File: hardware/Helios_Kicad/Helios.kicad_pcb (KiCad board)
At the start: 2 copper layers, 75 x 61 mm, 95 parts, among them P1 USB_B, P2 CONN_01X25-SHIELD, P3 CONN_01X03, U1 IP4220CZ6, U2 AP2114, U3 AN431B, U4 ISA_DC-DC_converter, U5 DAC084S085C, U6 TL084_v, U7 LM358, U8 TL084_v, U9 ATSAM4S, Y1 16MHz 18pF

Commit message: driver finished but untested
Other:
- board text added: "EMIT"
- board text removed: "LASER"
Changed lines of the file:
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@@
-(kicad_pcb (version 4) (host pcbnew 4.0.2-stable)
+(kicad_pcb (version 4) (host pcbnew 4.0.1-stable)
   (general
     (links 218)
@@
   )
   (setup
-    (last_trace_width 0.5)
+    (last_trace_width 0.35)
     (user_trace_width 0.25)
     (user_trace_width 0.35)
@@
       (solder_mask_margin 0.77) (clearance 0.77))
   )
-  (gr_line (start 101.1 117.5) (end 100.9 117.5) (angle 90) (layer F.SilkS) (width 0.2))
-  (gr_line (start 108.5 117.5) (end 101.1 117.5) (angle 90) (layer F.SilkS) (width 0.2))
-  (gr_line (start 108.5 123.3) (end 108.5 117.5) (angle 90) (layer F.SilkS) (width 0.2))
+  (gr_line (start 107 117.6) (end 107 118.2) (angle 90) (layer F.SilkS) (width 0.2))
+  (gr_line (start 107 117.6) (end 101 117.6) (angle 90) (layer F.SilkS) (width 0.2))
+  (gr_line (start 106.976 123.808) (end 106.976 118.008) (angle 90) (layer F.SilkS) (width 0.2))
   (gr_line (start 106.5 145.5) (end 106.5 139.4) (angle 90) (layer F.SilkS) (width 0.2))
   (gr_line (start 101 145.5) (end 106.5 145.5) (angle 90) (layer F.SilkS) (width 0.2))
-  (gr_text LASER (at 104.4 119.3) (layer F.SilkS)
+  (gr_text EMIT (at 103.6 119.4) (layer F.SilkS)
     (effects (font (size 1.5 1.5) (thickness 0.3)))
   )
@@
   (segment (start 123.6 111.2) (end 127.96 111.2) (width 0.6) (layer F.Cu) (net 4))
   (segment (start 127.96 111.2) (end 128.04 111.28) (width 0.6) (layer F.Cu) (net 4))
-  (segment (start 118.6 112.3) (end 122.3 112.3) (width 0.6) (layer F.Cu) (net 4))
-  (segment (start 122.3 112.3) (end 123.4 111.2) (width 0.6) (layer F.Cu) (net 4))
+  (segment (start 118.6 112.3) (end 122.3 112.3) (width 0.5) (layer F.Cu) (net 4))
+  (segment (start 122.3 112.3) (end 123.4 111.2) (width 0.5) (layer F.Cu) (net 4))
   (segment (start 123.4 111.2) (end 123.6 111.2) (width 0.6) (layer F.Cu) (net 4))
   (segment (start 118.6 111) (end 118.6 112.3) (width 0.6) (layer F.Cu) (net 4))

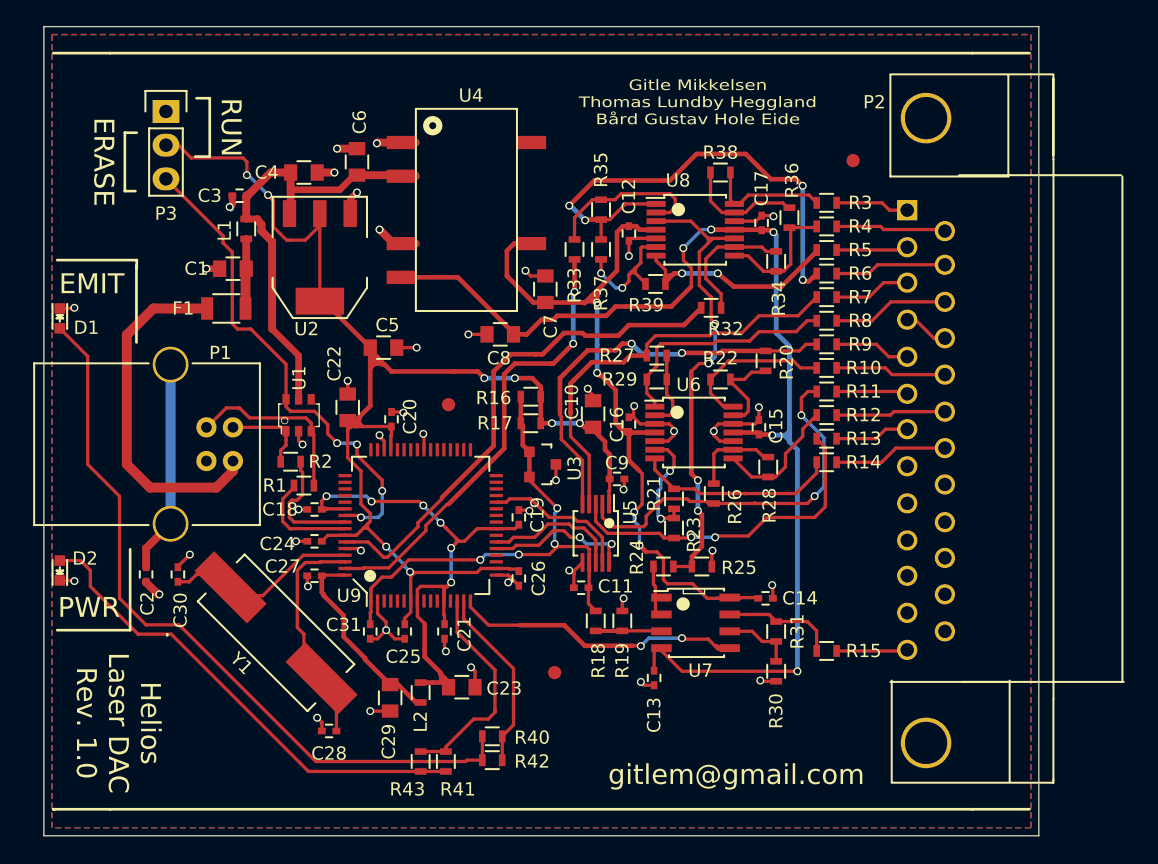
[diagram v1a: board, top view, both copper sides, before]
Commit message: GPIO signal wiring and USB IDs
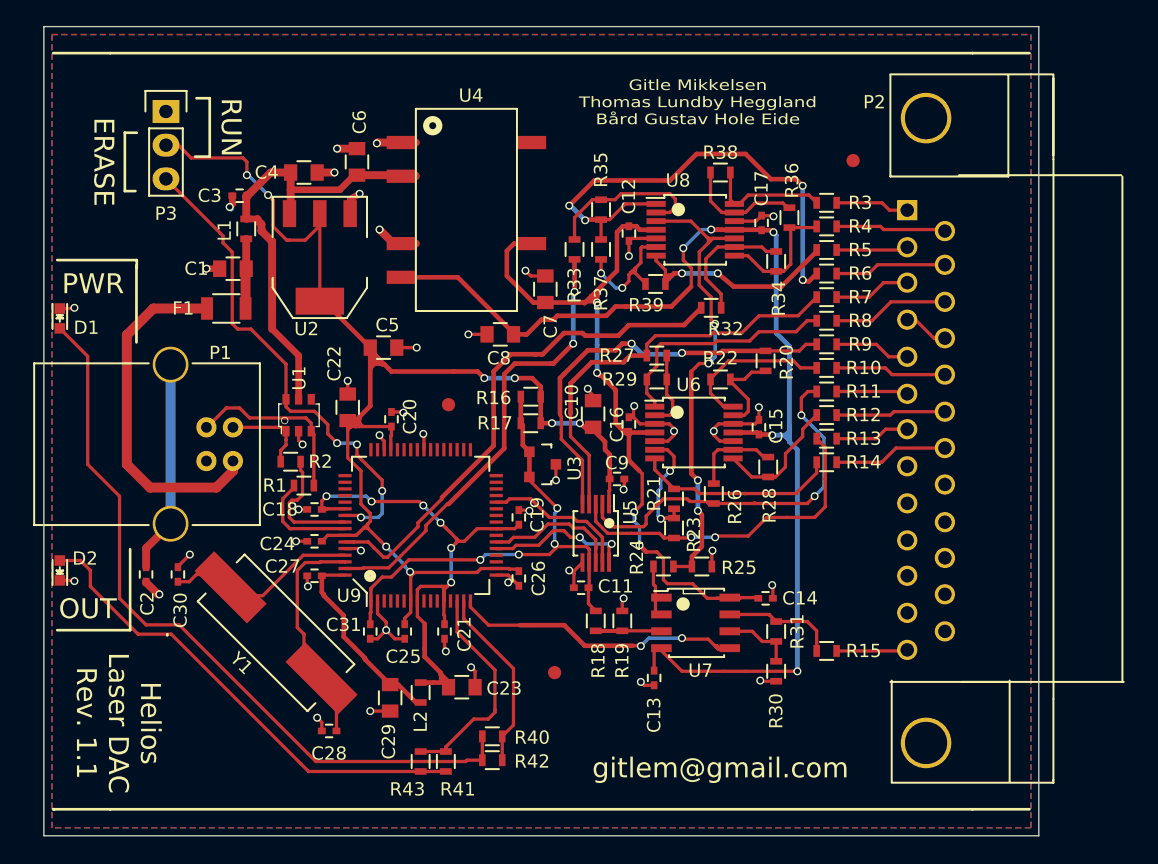
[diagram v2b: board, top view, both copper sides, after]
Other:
- board text added: "Helios Laser DAC Rev. 1.1"
- board text added: "OUT"
- board text removed: "EMIT"
- board text removed: "Helios Laser DAC Rev. 1.0"
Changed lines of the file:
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@@
-(kicad_pcb (version 4) (host pcbnew 4.0.1-stable)
+(kicad_pcb (version 4) (host pcbnew 4.0.2-stable)
   (general
     (links 218)
@@
   )
   (setup
-    (last_trace_width 0.35)
+    (last_trace_width 0.25)
     (user_trace_width 0.25)
     (user_trace_width 0.35)
@@
   (gr_line (start 106.5 145.5) (end 106.5 139.4) (angle 90) (layer F.SilkS) (width 0.2))
   (gr_line (start 101 145.5) (end 106.5 145.5) (angle 90) (layer F.SilkS) (width 0.2))
-  (gr_text EMIT (at 103.6 119.4) (layer F.SilkS)
+  (gr_text OUT (at 103.3 143.9) (layer F.SilkS)
     (effects (font (size 1.5 1.5) (thickness 0.3)))
   )
   (gr_line (start 109.3 145.9) (end 109.3 145.8) (angle 90) (layer F.SilkS) (width 0.2))
-  (gr_text PWR (at 103.4 143.8) (layer F.SilkS)
+  (gr_text PWR (at 103.7 119.4) (layer F.SilkS)
     (effects (font (size 1.5 1.5) (thickness 0.3)))
   )
-  (gr_text gitlem@gmail.com (at 152.2 156.4) (layer F.SilkS)
+  (gr_text gitlem@gmail.com (at 151 155.9) (layer F.SilkS)
     (effects (font (size 1.5 1.5) (thickness 0.3)))
   )
@@
   (gr_line (start 105 159) (end 100.7 159) (angle 90) (layer F.SilkS) (width 0.2))
   (gr_line (start 105 102) (end 100.7 102) (angle 90) (layer F.SilkS) (width 0.2))
-  (gr_text "Helios\nLaser DAC\nRev. 1.0" (at 105.6 152.5 270) (layer F.SilkS)
+  (gr_text "Helios\nLaser DAC\nRev. 1.1" (at 105.6 152.5 270) (layer F.SilkS)
     (effects (font (size 1.5 1.5) (thickness 0.3)))
   )
@@
   (segment (start 115.25 118.25) (end 115.25 116) (width 0.6) (layer F.Cu) (net 1))
   (segment (start 123.086 114.098) (end 123.086 113.014) (width 0.5) (layer F.Cu) (net 2))
-  (via (at 123.6 112.5) (size 0.6) (drill 0.4) (layers F.Cu B.Cu) (net 2))
-  (segment (start 123.086 113.014) (end 123.6 112.5) (width 0.5) (layer F.Cu) (net 2))
+  (via (at 123.8 112.6) (size 0.6) (drill 0.4) (layers F.Cu B.Cu) (net 2))
+  (segment (start 123.086 113.014) (end 123.8 112.6) (width 0.5) (layer F.Cu) (net 2))
   (via (at 112.25 118.25) (size 0.6) (drill 0.4) (layers F.Cu B.Cu) (net 2))
   (segment (start 112.25 118.25) (end 112.3 118.2) (width 0.5) (layer B.Cu) (net 2))

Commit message: redone pcb, driver and firmware working-ish
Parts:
- removed ? (x3): Fiducial_1mm_Dia_2.54mm_Outer_CopperTop, Fiducials:Fiducial_1mm_Dia_2.54mm_Outer_CopperTop
- removed P3: CONN_01X03, Pin_Headers:Pin_Header_Straight_1x03
- added C32: 13pF, Capacitors_SMD:C_0402, F.Cu at (124.8, 145.8)
- added ERASE: CONN_01X02, Connect:PINHEAD1-2, F.Cu at (122.7, 128.2)
- added L3: FILTER, Resistors_SMD:R_0603, F.Cu at (127.0, 149.2)
- added R44: 10k, Resistors_SMD:R_0603, F.Cu at (157.1, 114.9)
- added R45: 1.65k, Resistors_SMD:R_0603, F.Cu at (109.9, 153.6)
- added R46: 1.65k, Resistors_SMD:R_0603, F.Cu at (109.9, 151.7)
- added R47: 1.65k, Resistors_SMD:R_0603, F.Cu at (106.0, 147.3)
- added R48: 1.65k, Resistors_SMD:R_0603, F.Cu at (106.0, 145.5)
- C1, C23, C4, C5, C6, C8: footprint Capacitors_SMD:C_0805 -> Capacitors_SMD:C_0603
- C10, C22, C7: value 4.7uF -> 100nF; footprint Capacitors_SMD:C_0805 -> Capacitors_SMD:C_0402
- C11, C30: value 13pF -> 4.7uF; footprint Capacitors_SMD:C_0402 -> Capacitors_SMD:C_0603
- C12: value 100nF -> 13pF
- C24, C9: value 100nF -> 4.7uF; footprint Capacitors_SMD:C_0402 -> Capacitors_SMD:C_0603
- C28: value 13pF -> 100nF
- C29: value 4.7uF -> 13pF; footprint Capacitors_SMD:C_0805 -> Capacitors_SMD:C_0402
- F1: value PTC -> F_Small
- L1, L2: value FERRITE_BEAD -> FILTER
- R14, R15: value 150 -> 10k
- R16, R17: value 150 -> 5.11k
- R22, R34, R35, R36: value 10k -> 1.65k
- R24, R32, R41, R42: value 1.65k -> 5.11k
- R25, R30: value 10k -> 5.11k
- R31: value 5.11k -> 10k
- R40, R43: value 1.65k -> 10k
- U2: footprint SOT-223 -> TO_SOT_Packages_SMD:SOT-223
- U7: footprint SOIC-8_3.9x4.9mm_Pitch1.27mm -> personal:SOIC-8_3.9x4.9mm_Pitch1.27mm
- moved R41 53.5 mm to (151.7, 106.4), turned to 90 degrees
- moved R43 53.4 mm to (158.9, 111.6), turned to 90 degrees
- moved C18 44.5 mm to (153.3, 106.5), turned to 270 degrees
- moved R42 43.0 mm to (154.9, 117.8), turned to 270 degrees
- moved R40 42.5 mm to (156.7, 117.7), turned to 270 degrees
- moved L2 38.5 mm to (123.0, 112.1), turned to 0 degrees
- moved R15 28.3 mm to (140.6, 125.6)
- moved R13 24.6 mm to (134.5, 128.6), turned to 0 degrees
- moved R12 24.5 mm to (134.5, 130.4), turned to 0 degrees
- moved C12 23.6 mm to (138.7, 138.6), turned to 270 degrees
- moved C2 19.7 mm to (107.4, 121.6), turned to 90 degrees
- moved R11 19.6 mm to (162.3, 146.8), turned to 90 degrees
- moved C23 19.5 mm to (130.8, 130.3), turned to 180 degrees
- moved R14 19.2 mm to (140.6, 127.4), turned to 0 degrees
- moved C22 18.9 mm to (129.9, 146.3), turned to 270 degrees
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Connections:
- C11 pad 1: GND -> /DAC/3.3V
- C11 pad 2: /Amplifiers/2.5V -> GND
- C12 pad 2: /Amplifiers/+9V -> /Amplifiers/2.5V
- C13 pad 2: /Amplifiers/-9V -> /Amplifiers/+9V
- C14 pad 2: /Amplifiers/+9V -> /Amplifiers/-9V
- C15 pad 2: /Amplifiers/-9V -> /Amplifiers/+9V
- C16 pad 2: /Amplifiers/+9V -> /Amplifiers/-9V
- C17 pad 2: /Amplifiers/-9V -> /Amplifiers/+9V
- C18 pad 1: /Microcontroller/VDDOUT -> GND
- C18 pad 2: GND -> /Amplifiers/-9V
- C20 pad 1: /DAC/3.3V -> /Microcontroller/VDDOUT
- C21 pad 1: /Microcontroller/VDDOUT -> /DAC/3.3V
- C22 pad 1: /DAC/3.3V -> /Microcontroller/VDDOUT
- C23 pad 1: /Microcontroller/VDDOUT -> /DAC/3.3V
- C24 pad 1: /DAC/3.3V -> /Microcontroller/VDDOUT
- C27 pad 1: /Microcontroller/VDDPLL -> /DAC/3.3V
- C28 pad 1: /Microcontroller/XIN -> /Microcontroller/VDDPLL
- C29 pad 1: /Microcontroller/VDDPLL -> /Microcontroller/XIN
- C30 pad 1: /Microcontroller/XOUT -> /Microcontroller/VDDPLL
- C31 pad 1: /Amplifiers/2.5V -> /Microcontroller/XOUT
- C7 pad 1: GND -> Net-(C7-Pad1)
- C7 pad 2: /Amplifiers/+9V -> GND
- C8 pad 1: /Amplifiers/-9V -> GND
- C8 pad 2: GND -> /Amplifiers/+9V
- C9 pad 1: /DAC/3.3V -> /Amplifiers/-9V
- L2 pad 1: /Microcontroller/VDDOUT -> /Power Regulation/5V
- L2 pad 2: /Microcontroller/VDDPLL -> Net-(C7-Pad1)
- P2 pad 16: Net-(P2-Pad16) -> GND
- P2 pad 18: Net-(P2-Pad18) -> GND
- P2 pad 19: Net-(P2-Pad19) -> GND
- P2 pad 20: Net-(P2-Pad20) -> GND
- R10 pad 1: Net-(P2-Pad18) -> Net-(P2-Pad7)
- R10 pad 2: /Amplifiers/-R -> /Amplifiers/+B
- R11 pad 1: Net-(P2-Pad6) -> Net-(P2-Pad13)
- R11 pad 2: /Amplifiers/+G -> /Amplifiers/Shutter_Out
- R12 pad 1: Net-(P2-Pad19) -> /DAC/3.3V
- R12 pad 2: /Amplifiers/-G -> /Amplifiers/2.5V
- R13 pad 1: Net-(P2-Pad7) -> /DAC/3.3V
- R13 pad 2: /Amplifiers/+B -> /Amplifiers/2.5V
- R14 pad 1: Net-(P2-Pad20) -> /Amplifiers/2.5V
- R14 pad 2: /Amplifiers/-B -> Net-(R14-Pad2)
- R15 pad 1: Net-(P2-Pad13) -> Net-(R14-Pad2)
- R15 pad 2: /Amplifiers/Shutter_Out -> GND
- R16 pad 1: /DAC/3.3V -> Net-(R16-Pad1)
- R16 pad 2: /Amplifiers/2.5V -> /Amplifiers/R
- R17 pad 1: /DAC/3.3V -> Net-(R17-Pad1)
- R17 pad 2: /Amplifiers/2.5V -> /Amplifiers/B
- R18 pad 1: /Amplifiers/2.5V -> GND
- R19 pad 1: Net-(R18-Pad2) -> GND
- R19 pad 2: GND -> Net-(R19-Pad2)
- R20 pad 1: Net-(R20-Pad1) -> /Amplifiers/+R
- R20 pad 2: /Amplifiers/+R -> GND
- R21 pad 1: Net-(R21-Pad1) -> /Amplifiers/+B
- R21 pad 2: /Amplifiers/+B -> GND
- R22 pad 1: /Amplifiers/-R -> Net-(R22-Pad1)
- R22 pad 2: Net-(R20-Pad1) -> /Amplifiers/Offset
- R23 pad 1: /Amplifiers/-B -> /Amplifiers/Offset
- R23 pad 2: Net-(R21-Pad1) -> GND
- R24 pad 2: /Amplifiers/Offset -> /Amplifiers/G
- R25 pad 1: /Amplifiers/Offset -> Net-(R25-Pad1)
- R25 pad 2: GND -> /Amplifiers/Intensity
- R26 pad 1: Net-(R26-Pad1) -> GND
- R26 pad 2: /Amplifiers/+G -> Net-(R26-Pad2)
- R27 pad 1: Net-(R27-Pad1) -> GND
- R27 pad 2: /Amplifiers/+Intensity -> Net-(R27-Pad2)
- R28 pad 1: /Amplifiers/-G -> /Amplifiers/+Intensity
- R28 pad 2: Net-(R26-Pad1) -> GND
- R29 pad 1: /Amplifiers/-Intensity -> /Amplifiers/+G
- R29 pad 2: Net-(R27-Pad1) -> GND
- R30 pad 1: GND -> Net-(R30-Pad1)
- R30 pad 2: Net-(R30-Pad2) -> /Amplifiers/Shutter
- R31 pad 1: /Amplifiers/Shutter_Out -> GND
- R31 pad 2: Net-(R30-Pad2) -> Net-(R31-Pad2)
- R32 pad 1: Net-(R32-Pad1) -> /Amplifiers/Shutter_Out
- R32 pad 2: /Amplifiers/X -> Net-(R31-Pad2)
- R33 pad 2: /Amplifiers/Y -> /Amplifiers/Offset
- R34 pad 1: /Amplifiers/-X -> Net-(R34-Pad1)
- R34 pad 2: Net-(R32-Pad1) -> /Amplifiers/Offset
- R35 pad 1: /Amplifiers/-Y -> Net-(R35-Pad1)
- R35 pad 2: Net-(R33-Pad1) -> /Amplifiers/X
- R36 pad 2: /Amplifiers/-X -> /Amplifiers/Y
- R37 pad 1: Net-(R37-Pad1) -> /Amplifiers/-X
- R37 pad 2: /Amplifiers/-Y -> Net-(R35-Pad1)
- R38 pad 1: /Amplifiers/+X -> /Amplifiers/-Y
- R39 pad 1: /Amplifiers/+Y -> Net-(R39-Pad1)
- R39 pad 2: Net-(R37-Pad1) -> /Amplifiers/-X
- R40 pad 1: /Microcontroller/PA23 -> Net-(R40-Pad1)
- R40 pad 2: Net-(D1-Pad2) -> /Amplifiers/-Y
- R41 pad 1: /Microcontroller/PA22 -> Net-(R41-Pad1)
- R41 pad 2: Net-(D2-Pad2) -> GND
- R42 pad 1: /Microcontroller/PA23 -> Net-(R42-Pad1)
- R42 pad 2: Net-(D1-Pad2) -> GND
- R43 pad 1: /Microcontroller/PA22 -> /Amplifiers/+X
- R43 pad 2: Net-(D2-Pad2) -> Net-(R39-Pad1)
- R8 pad 1: Net-(P2-Pad16) -> Net-(P2-Pad5)
- R8 pad 2: /Amplifiers/-Intensity -> /Amplifiers/+R
- R9 pad 1: Net-(P2-Pad5) -> Net-(P2-Pad6)
- R9 pad 2: /Amplifiers/+R -> /Amplifiers/+G
- U1 pad 6: /Microcontroller/ERASE -> (no net)
- U4 pad 2: /Power Regulation/5V -> Net-(C7-Pad1)
- U5 pad 2: /Amplifiers/+G -> /Amplifiers/Intensity
- U5 pad 3: /Amplifiers/+B -> /Amplifiers/B
- U5 pad 4: /Amplifiers/+Intensity -> /Amplifiers/G
- U5 pad 5: /Amplifiers/+R -> /Amplifiers/R
- U6 pad 1: /Amplifiers/-Intensity -> /Amplifiers/+Intensity
- U6 pad 10: GND -> Net-(R24-Pad1)
- U6 pad 12: GND -> Net-(R16-Pad1)
- U6 pad 13: Net-(R20-Pad1) -> Net-(R18-Pad2)
- U6 pad 14: /Amplifiers/-R -> /Amplifiers/+R
- U6 pad 2: Net-(R27-Pad1) -> Net-(R26-Pad2)
- U6 pad 3: GND -> Net-(R25-Pad1)
- U6 pad 5: GND -> Net-(R17-Pad1)
- U6 pad 6: Net-(R21-Pad1) -> Net-(R19-Pad2)
- U6 pad 7: /Amplifiers/-B -> /Amplifiers/+B
- U6 pad 8: /Amplifiers/-G -> /Amplifiers/+G
- U6 pad 9: Net-(R26-Pad1) -> Net-(R27-Pad2)
- U7 pad 1: Net-(R24-Pad1) -> Net-(R22-Pad1)
- U7 pad 2: Net-(R24-Pad1) -> Net-(R22-Pad1)
- U7 pad 3: Net-(R18-Pad2) -> Net-(R14-Pad2)
- U7 pad 5: /Amplifiers/Shutter -> Net-(R30-Pad1)
- U7 pad 6: Net-(R30-Pad2) -> Net-(R31-Pad2)
- U8 pad 10: /Amplifiers/Offset -> Net-(R34-Pad1)
- U8 pad 12: GND -> Net-(R41-Pad1)
- U8 pad 13: Net-(R36-Pad1) -> Net-(R39-Pad1)
- U8 pad 2: Net-(R33-Pad1) -> Net-(R36-Pad1)
- U8 pad 3: /Amplifiers/Offset -> Net-(R33-Pad1)
- U8 pad 5: GND -> Net-(R42-Pad1)
- U8 pad 6: Net-(R37-Pad1) -> Net-(R40-Pad1)
- U8 pad 9: Net-(R32-Pad1) -> Net-(R35-Pad1)
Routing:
- net /Amplifiers/Shutter_Out: track 8.93 -> 45.7 mm
- net /Microcontroller/PA22: track 16.6 -> 44.2 mm
- net Net-(D2-Pad2): track 36.4 -> 9.74 mm
- net /Microcontroller/ERASE: track 37.5 -> 11.2 mm, vias 4 -> 0
- net /Microcontroller/PA23: track 13.9 -> 38.7 mm
- net /Amplifiers/-Y: track 37.7 -> 15.3 mm, vias 4 -> 0
- net Net-(D1-Pad2): track 56.5 -> 35.7 mm
- net /Amplifiers/Offset: track 35.6 -> 17.3 mm, vias 4 -> 0
- net /DAC/3.3V: track 111.2 -> 92.9 mm, vias 8 -> 2
- net /Amplifiers/-Intensity: track 17.9 -> 0.00 mm
- net /Amplifiers/-9V: track 87.9 -> 71.2 mm, vias 5 -> 4
- net /Amplifiers/-B: track 15.4 -> 0.00 mm
- net /Amplifiers/+G: track 29.0 -> 15.1 mm
- net /Amplifiers/2.5V: track 38.4 -> 50.6 mm
- net /Amplifiers/Y: track 34.1 -> 46.2 mm, vias 2 -> 4
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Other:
- board size 75 x 61 mm -> 75.2 x 61.1 mm
- net class Power removed
- board text added: "Gitle Mikkelsen Thomas L Heggland Bård Gustav Hole Eide"
- board text added: "Helios Laser DAC Rev 1.1"
- board text removed: "ERASE"
- board text removed: "Gitle Mikkelsen Thomas Lundby Heggland Bård Gustav Hole Eide"
- board text removed: "Helios Laser DAC Rev. 1.1"
- board text removed: "OUT"
- board text removed: "PWR"
- board text removed: "RUN"

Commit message: rev 1.1 pcb final
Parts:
- removed C5: 4.7uF, Capacitors_SMD:C_0603
- added REF**: Fiducial_1mm_Dia_2.54mm_Outer_CopperTop, Fiducials:Fiducial_1mm_Dia_2.54mm_Outer_CopperTop, F.Cu at (104.3, 108.5)
- added REF**: Fiducial_1mm_Dia_2.54mm_Outer_CopperTop, Fiducials:Fiducial_1mm_Dia_2.54mm_Outer_CopperTop, F.Cu at (142.2, 106.0)
- added REF**: Fiducial_1mm_Dia_2.54mm_Outer_CopperTop, Fiducials:Fiducial_1mm_Dia_2.54mm_Outer_CopperTop, F.Cu at (140.7, 149.7)
- C1, C11, C23, C24, C30, C4, C6, C8, C9: footprint Capacitors_SMD:C_0603 -> Capacitors_SMD:c_elec_4x5.3
- moved C4 8.72 mm to (110.9, 109.0)
- moved C23 6.50 mm to (126.7, 125.2), turned to 270 degrees
- moved C1 4.27 mm to (107.4, 115.5), turned to 0 degrees
- moved C24 3.19 mm to (132.4, 151.2), turned to 90 degrees
- moved C11 3.03 mm to (143.8, 134.6), turned to 270 degrees
- moved C30 2.89 mm to (125.2, 151.3)
- moved C8 2.25 mm to (141.9, 114.0)
- moved C6 2.06 mm to (118.7, 110.3), turned to 270 degrees
- moved L3 1.75 mm to (128.8, 149.2), turned to 270 degrees
- moved Y1 1.69 mm to (115.5, 144.9)
- moved C9 1.15 mm to (132.8, 123.4), turned to 0 degrees
- moved L1 1.12 mm to (112.8, 115.1)
- moved C28 0.51 mm to (121.0, 143.8)
- moved F1 0.45 mm to (112.5, 120.3)
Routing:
- net /Power Regulation/5V: track 29.8 -> 35.6 mm
- net GND: track 69.0 -> 73.7 mm, vias 48 -> 49
- net /D-: track 7.38 -> 11.6 mm
- net /Microcontroller/PA23: track 38.7 -> 42.9 mm
- net /Microcontroller/PA22: track 44.2 -> 48.3 mm
- net Net-(C1-Pad1): track 4.31 -> 6.75 mm
- net /DAC/3.3V: track 92.9 -> 95.3 mm
- net /Microcontroller/VDDPLL: track 12.2 -> 14.4 mm
- net /Amplifiers/-9V: track 71.2 -> 73.0 mm
- net /Microcontroller/VDDOUT: track 33.8 -> 35.4 mm
- net /Microcontroller/XOUT: track 10.8 -> 11.9 mm
- net /Amplifiers/2.5V: track 50.6 -> 51.6 mm
- net /Microcontroller/D-: track 6.84 -> 7.53 mm
- net /DAC/Din: track 6.60 -> 7.27 mm
- net /Amplifiers/X: track 45.1 -> 44.5 mm
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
